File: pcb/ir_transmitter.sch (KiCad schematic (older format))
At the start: 6 parts, among them IC9 NJM2746, Q1 IRFML8244

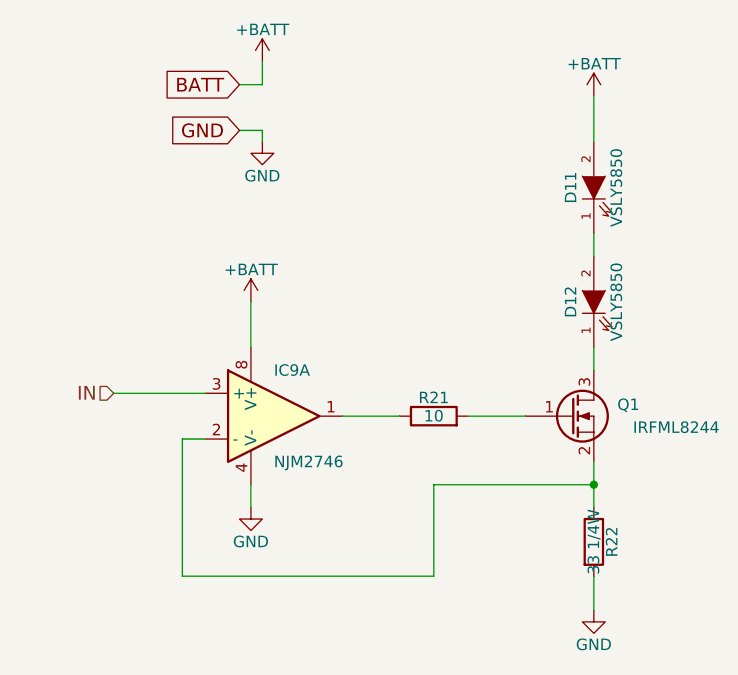
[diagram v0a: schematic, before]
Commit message: 回路図を修正 ・赤外線LEDの発光回路にpull down抵抗を追加 ・赤外線LEDの発光回路の電流制限抵抗の値を変更
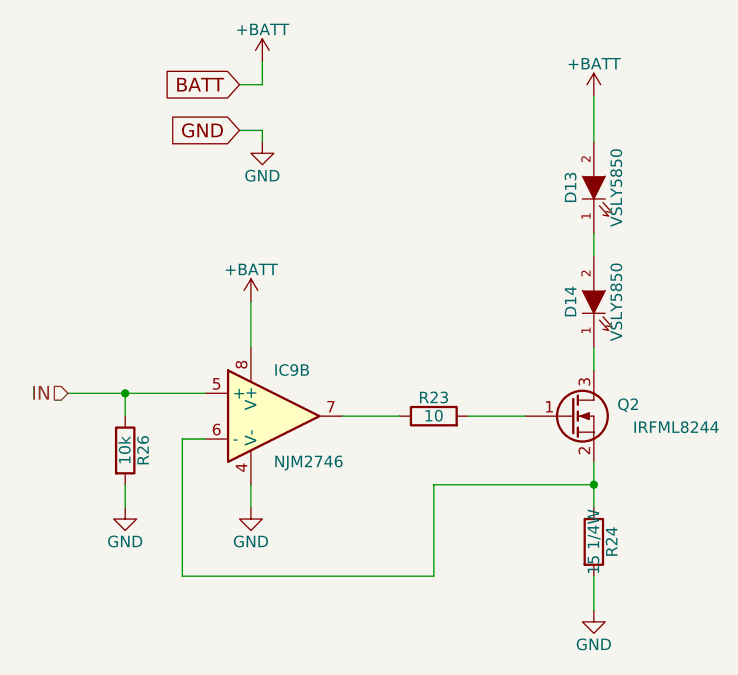
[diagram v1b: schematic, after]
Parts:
- added R25: 10k, Resistors_SMD:R_0603, symbol R
- R22: value 33 1/4W -> 15 1/4W
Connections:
- net GND: now also R25.2
- net IN: now also IC9.5 (+), R25.1; no longer IC9.3 (+)
- net at R21.1: now also IC9.7; no longer IC9.1
- net at Q1.2 (S), R22.1: now also IC9.6 (-); no longer IC9.2 (-)
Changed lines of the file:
@@
 $Descr A4 11693 8268
 encoding utf-8
-Sheet 11 12
+Sheet 12 12
 Title ""
 Date ""
@@
 AR Path="/57CD846F/57DFA47C" Ref="R21"  Part="1"
 AR Path="/57E50252/57DFA47C" Ref="R23"  Part="1"
-F 0 "R21" V 6230 4550 50  0000 C CNN
+F 0 "R23" V 6230 4550 50  0000 C CNN
 F 1 "10" V 6150 4550 50  0000 C CNN
 F 2 "Resistors_SMD:R_0603" V 6080 4550 50  0001 C CNN
@@
 AR Path="/57CD846F/57DFA4DB" Ref="Q1"  Part="1"
 AR Path="/57E50252/57DFA4DB" Ref="Q2"  Part="1"
-F 0 "Q1" H 7050 4600 50  0000 R CNN
+F 0 "Q2" H 7050 4600 50  0000 R CNN
 F 1 "IRFML8244" H 7400 4500 50  0000 R CNN
 F 2 "TO_SOT_Packages_SMD:SOT-23" H 6950 4650 50  0001 C CNN
@@
 AR Path="/57CD846F/57DFA512" Ref="D12"  Part="1"
 AR Path="/57E50252/57DFA512" Ref="D14"  Part="1"
-F 0 "D12" H 6850 4150 50  0000 C CNN
+F 0 "D14" H 6850 4150 50  0000 C CNN
 F 1 "VSLY5850" H 6850 3950 50  0000 C CNN
 F 2 "micromouse2016:LED_5mm_angle" H 6850 4050 50  0001 C CNN
@@
 AR Path="/57CD846F/57DFA58F" Ref="D11"  Part="1"
 AR Path="/57E50252/57DFA58F" Ref="D13"  Part="1"
-F 0 "D11" H 6850 3650 50  0000 C CNN
+F 0 "D13" H 6850 3650 50  0000 C CNN
 F 1 "VSLY5850" H 6850 3450 50  0000 C CNN
 F 2 "micromouse2016:LED_5mm_angle" H 6850 3550 50  0001 C CNN
@@
 AR Path="/57CD846F/57DFA5ED" Ref="R22"  Part="1"
 AR Path="/57E50252/57DFA5ED" Ref="R24"  Part="1"
-F 0 "R22" V 6930 5100 50  0000 C CNN
-F 1 "33 1/4W" V 6850 5100 50  0000 C CNN
+F 0 "R24" V 6930 5100 50  0000 C CNN
+F 1 "15 1/4W" V 6850 5100 50  0000 C CNN
 F 2 "Resistors_SMD:R_1206" V 6780 5100 50  0001 C CNN
 F 3 "" H 6850 5100 50  0000 C CNN
@@
 P 6850 5400
 AR Path="/57CD846F/57DFA62F" Ref="#PWR0116"  Part="1"
-AR Path="/57E50252/57DFA62F" Ref="#PWR0122"  Part="1"
-F 0 "#PWR0116" H 6850 5150 50  0001 C CNN
+AR Path="/57E50252/57DFA62F" Ref="#PWR0123"  Part="1"
+F 0 "#PWR0123" H 6850 5150 50  0001 C CNN
 F 1 "GND" H 6850 5250 50  0000 C CNN
 F 2 "" H 6850 5400 50  0000 C CNN
@@
 P 5350 4950
 AR Path="/57CD846F/57DFA771" Ref="#PWR0117"  Part="1"
-AR Path="/57E50252/57DFA771" Ref="#PWR0123"  Part="1"
-F 0 "#PWR0117" H 5350 4700 50  0001 C CNN
+AR Path="/57E50252/57DFA771" Ref="#PWR0124"  Part="1"
+F 0 "#PWR0124" H 5350 4700 50  0001 C CNN
 F 1 "GND" H 5350 4800 50  0000 C CNN
 F 2 "" H 5350 4950 50  0000 C CNN
@@
 	1    0    0    -1
 $EndComp
-Text HLabel 4750 4450 0    60   Input ~ 0
+Text HLabel 4550 4450 0    60   Input ~ 0
 IN
 Text GLabel 5300 3100 0    60   Input ~ 0
@@
 P 5350 4050
 AR Path="/57CD846F/57DFB316" Ref="#PWR0118"  Part="1"
-AR Path="/57E50252/57DFB316" Ref="#PWR0124"  Part="1"
-F 0 "#PWR0118" H 5350 3900 50  0001 C CNN
+AR Path="/57E50252/57DFB316" Ref="#PWR0125"  Part="1"
+F 0 "#PWR0125" H 5350 3900 50  0001 C CNN
 F 1 "+BATT" H 5350 4190 50  0000 C CNN
 F 2 "" H 5350 4050 50  0000 C CNN
@@
 P 6850 3150
 AR Path="/57CD846F/57DFB388" Ref="#PWR0119"  Part="1"
-AR Path="/57E50252/57DFB388" Ref="#PWR0125"  Part="1"
-F 0 "#PWR0119" H 6850 3000 50  0001 C CNN
+AR Path="/57E50252/57DFB388" Ref="#PWR0126"  Part="1"
+F 0 "#PWR0126" H 6850 3000 50  0001 C CNN
 F 1 "+BATT" H 6850 3290 50  0000 C CNN
 F 2 "" H 6850 3150 50  0000 C CNN
@@
 P 5400 3000
 AR Path="/57CD846F/57DFB3E2" Ref="#PWR0120"  Part="1"
-AR Path="/57E50252/57DFB3E2" Ref="#PWR0126"  Part="1"
-F 0 "#PWR0120" H 5400 2850 50  0001 C CNN
+AR Path="/57E50252/57DFB3E2" Ref="#PWR0127"  Part="1"
+F 0 "#PWR0127" H 5400 2850 50  0001 C CNN
 F 1 "+BATT" H 5400 3140 50  0000 C CNN
 F 2 "" H 5400 3000 50  0000 C CNN
@@
 P 5400 3350
 AR Path="/57CD846F/57DFB42F" Ref="#PWR0121"  Part="1"
-AR Path="/57E50252/57DFB42F" Ref="#PWR0127"  Part="1"
-F 0 "#PWR0121" H 5400 3100 50  0001 C CNN
+AR Path="/57E50252/57DFB42F" Ref="#PWR0128"  Part="1"
+F 0 "#PWR0128" H 5400 3100 50  0001 C CNN
 F 1 "GND" H 5400 3200 50  0000 C CNN
 F 2 "" H 5400 3350 50  0000 C CNN
@@
 $Comp
 L NJM2746 IC9
-U 1 1 57DFA459
+U 2 1 57DFA459
 P 5450 4550
 AR Path="/57CD846F/57DFA459" Ref="IC9"  Part="1"
@@
 F 2 "Housings_SSOP:TSSOP-8_4.4x3mm_Pitch0.65mm" H 5450 4550 50  0001 C CNN
 F 3 "" H 5450 4550 50  0000 C CNN
-	1    5450 4550
+	2    5450 4550
 	1    0    0    -1
 $EndComp
@@
 Connection ~ 6850 4850
 Wire Wire Line
-	4750 4450 5150 4450
+	4550 4450 5150 4450
 Wire Wire Line
 	5300 3100 5400 3100
@@
 Wire Wire Line
 	5350 4050 5350 4250
+$Comp
+L R R25
+U 1 1 5836E11C
+P 4800 4700
+AR Path="/57CD846F/5836E11C" Ref="R25"  Part="1"
+AR Path="/57E50252/5836E11C" Ref="R26"  Part="1"
+F 0 "R26" V 4880 4700 50  0000 C CNN
+F 1 "10k" V 4800 4700 50  0000 C CNN
+F 2 "Resistors_SMD:R_0603" V 4730 4700 50  0001 C CNN
+F 3 "" H 4800 4700 50  0000 C CNN
+	1    4800 4700
+	1    0    0    -1
+$EndComp
+$Comp
+L GND #PWR0129
+U 1 1 5836E1A4
+P 4800 4950
+AR Path="/57E50252/5836E1A4" Ref="#PWR0129"  Part="1"
+AR Path="/57CD846F/5836E1A4" Ref="#PWR0122"  Part="1"
+F 0 "#PWR0129" H 4800 4700 50  0001 C CNN
+F 1 "GND" H 4800 4800 50  0000 C CNN
+F 2 "" H 4800 4950 50  0000 C CNN
+F 3 "" H 4800 4950 50  0000 C CNN
+	1    4800 4950
+	1    0    0    -1
+$EndComp
+Wire Wire Line
+	4800 4950 4800 4850
+Wire Wire Line
+	4800 4550 4800 4450
+Connection ~ 4800 4450
 $EndSCHEMATC
